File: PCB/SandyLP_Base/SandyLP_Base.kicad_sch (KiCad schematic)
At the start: 180 parts, among them J1 Conn_01x10_Pin, J7 USB_C_Receptacle_USB2.0, J8 Conn_01x03, Q1 BSS138, SW1 BOOT, SW2 RESET, U1 NCP1117-3.3_SOT223, U2 RP2040, U3 W25Q128JVPIQ, Y1 12MHz

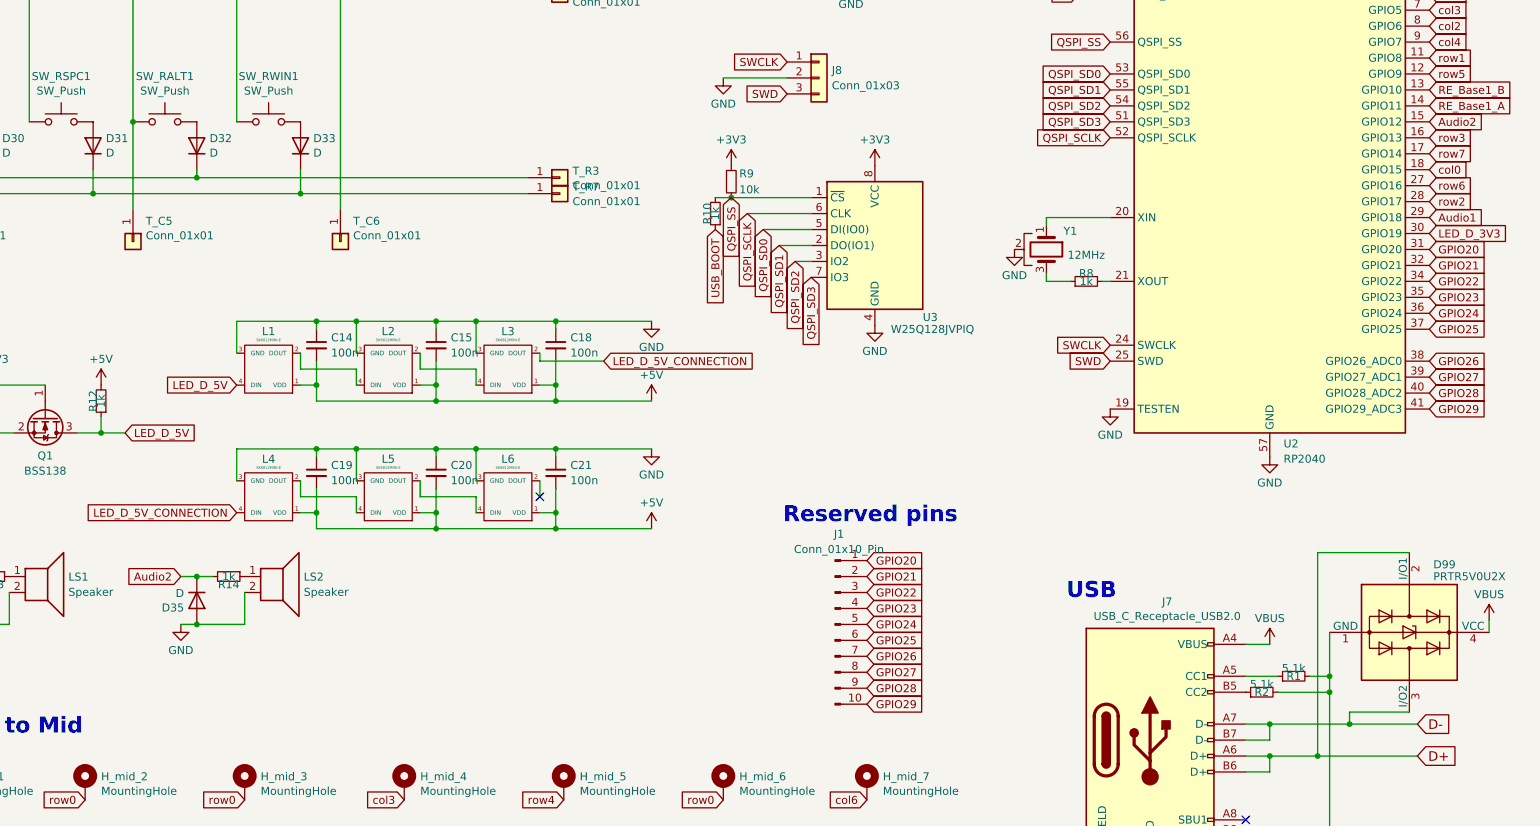
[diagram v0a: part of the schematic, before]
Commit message: issue セカンダリスピーカーを削除 #25
- スピーカー関連削除
- 未使用となったGPIO12をテストポイントとしてアクセス可能に
- 付近の配線、GNDベタ調整
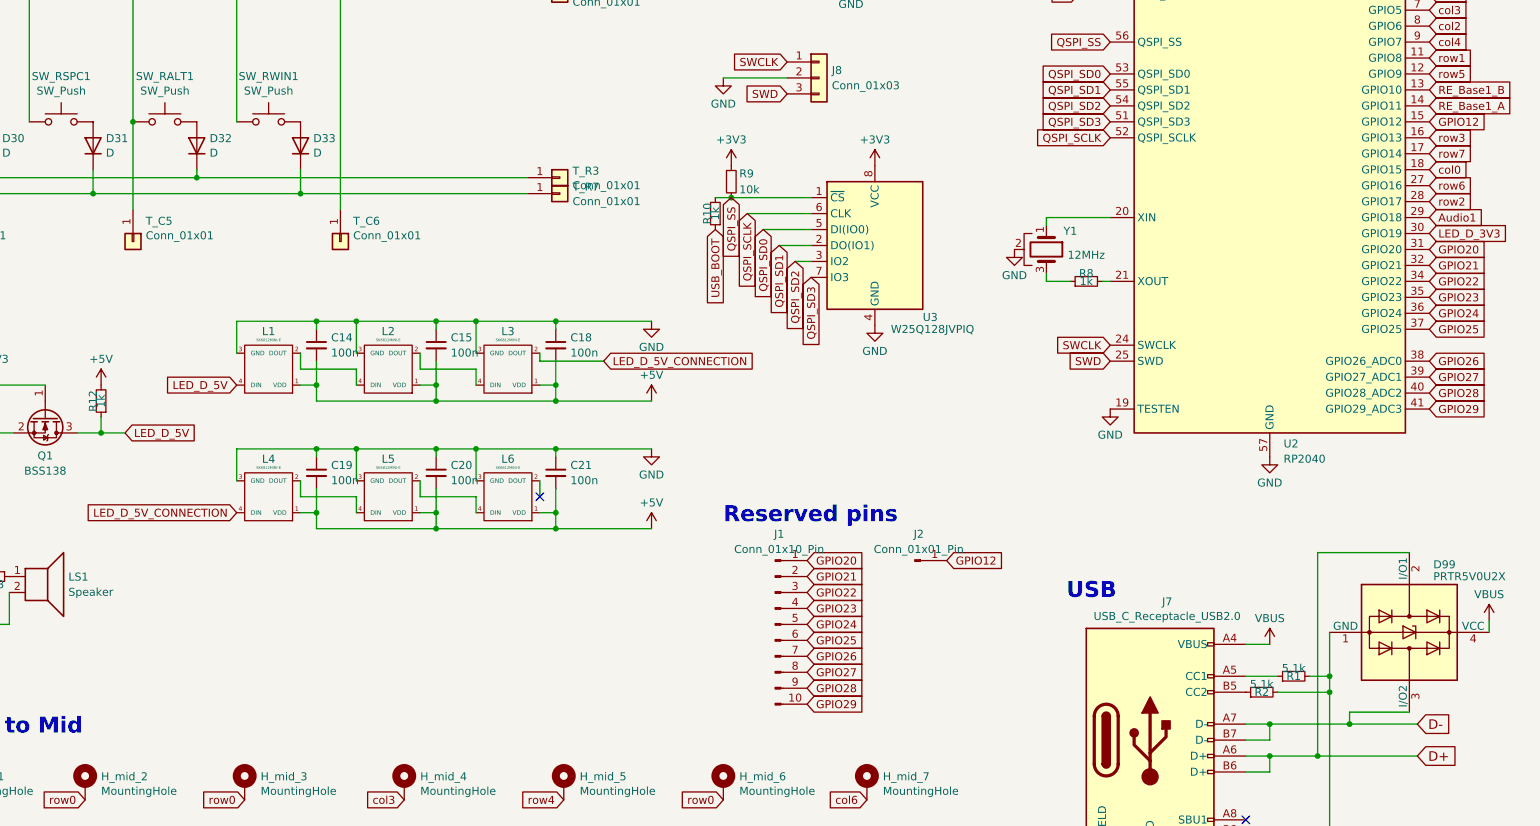
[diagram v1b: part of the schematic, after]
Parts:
- removed D35: D, locallib:D_SOD-123_Emphasized_Direction_Line_Reference_on_bottom, symbol Device:D
- removed LS2: Speaker, Buzzer_Beeper:Buzzer_Murata_PKMCS0909E, symbol Device:Speaker
- removed R14: 1k, Resistor_SMD:R_0402_1005Metric, symbol Device:R_Small
- added J2: Conn_01x01_Pin, TestPoint:TestPoint_THTPad_D1.0mm_Drill0.5mm, symbol Connector:Conn_01x01_Pin
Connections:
- net Audio2 renamed GPIO12
- net GPIO12: now also J2.1 (Pin_1)
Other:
- moved on the sheet: J1

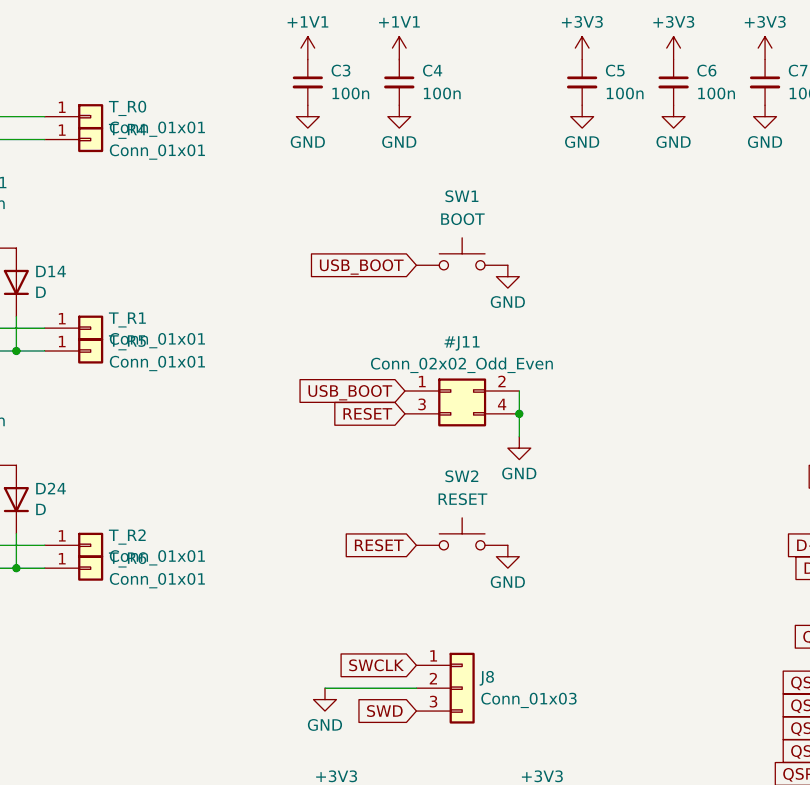
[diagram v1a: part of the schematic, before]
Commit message: issue BOOTSELスイッチを両対応 #28
PTS810スイッチを隣に並べた。
RESETスイッチは削除して、ピンヘッダに出した。
LEDはサイズを変更。
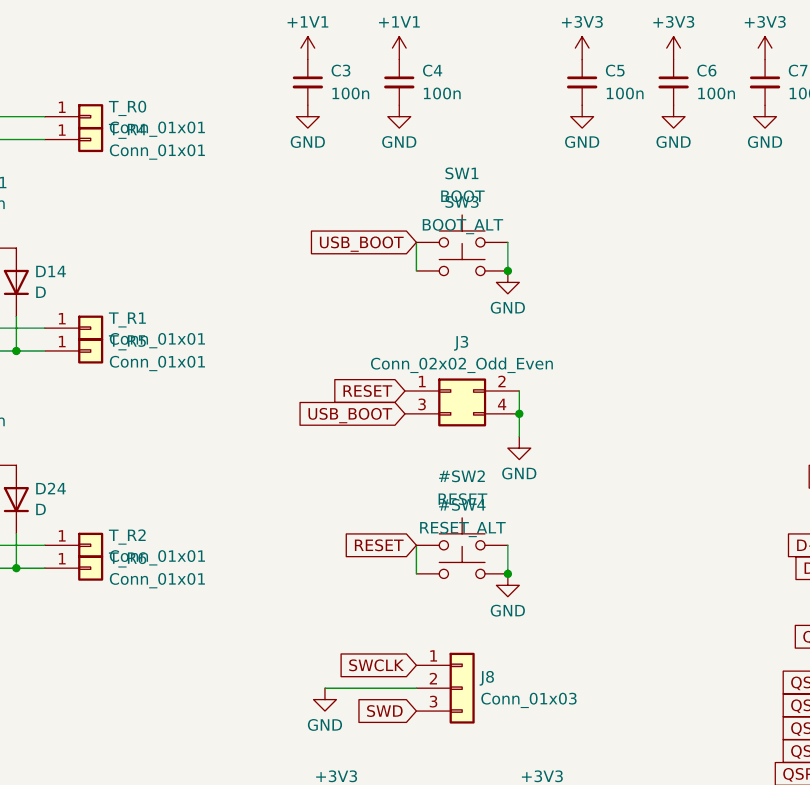
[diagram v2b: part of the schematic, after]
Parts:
- added #SW4: RESET_ALT, Button_Switch_SMD:SW_SPST_PTS810, symbol Switch:SW_Push
- added SW3: BOOT_ALT, Button_Switch_SMD:SW_SPST_PTS810, symbol Switch:SW_Push
- J3: renamed from #J11; footprint Connector_PinHeader_2.00mm:PinHeader_2x02_P2.00mm_Vertical -> locallib:PinHeader_2x02_P2.00mm_Vertical_2pair
- STLED1: footprint LED_SMD:LED_0402_1005Metric -> LED_SMD:LED_0201_0603Metric_Pad0.64x0.40mm_HandSolder; LCSC C130723 -> (none)
- renumbered SW2 to #SW2
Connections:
- net GND: now also #SW4.2, SW3.1
- net RESET: now also J3.1 (Pin_1), #SW4.1; no longer J3.3 (Pin_3)
- net USB_BOOT: now also J3.3 (Pin_3), SW3.2; no longer J3.1 (Pin_1)
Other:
- moved on the sheet: SW1

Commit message: C1,C2バーツ変更に伴う、チップサイズ変更。
JLCPCBのSMTAで、ExtendedからBasicのパーツに変更。
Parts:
- C1, C2: footprint Capacitor_SMD:C_1206_3216Metric -> Capacitor_SMD:C_0805_2012Metric; LCSC C77090 -> C15850
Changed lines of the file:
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@@
 			)
 		)
-		(property "Footprint" "Capacitor_SMD:C_1206_3216Metric"
+		(property "Footprint" "Capacitor_SMD:C_0805_2012Metric"
 			(at 345.44 25.4 0)
 			(effects
@@
 			)
 		)
-		(property "LCSC" "C77090"
+		(property "LCSC" "C15850"
 			(at 345.44 25.4 0)
 			(effects
@@
 			)
 		)
-		(property "Footprint" "Capacitor_SMD:C_1206_3216Metric"
+		(property "Footprint" "Capacitor_SMD:C_0805_2012Metric"
 			(at 318.77 25.4 0)
 			(effects
@@
 			)
 		)
-		(property "LCSC" "C77090"
+		(property "LCSC" "C15850"
 			(at 318.77 25.4 0)
 			(effects
